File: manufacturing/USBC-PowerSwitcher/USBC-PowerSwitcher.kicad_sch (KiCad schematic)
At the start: 0 parts

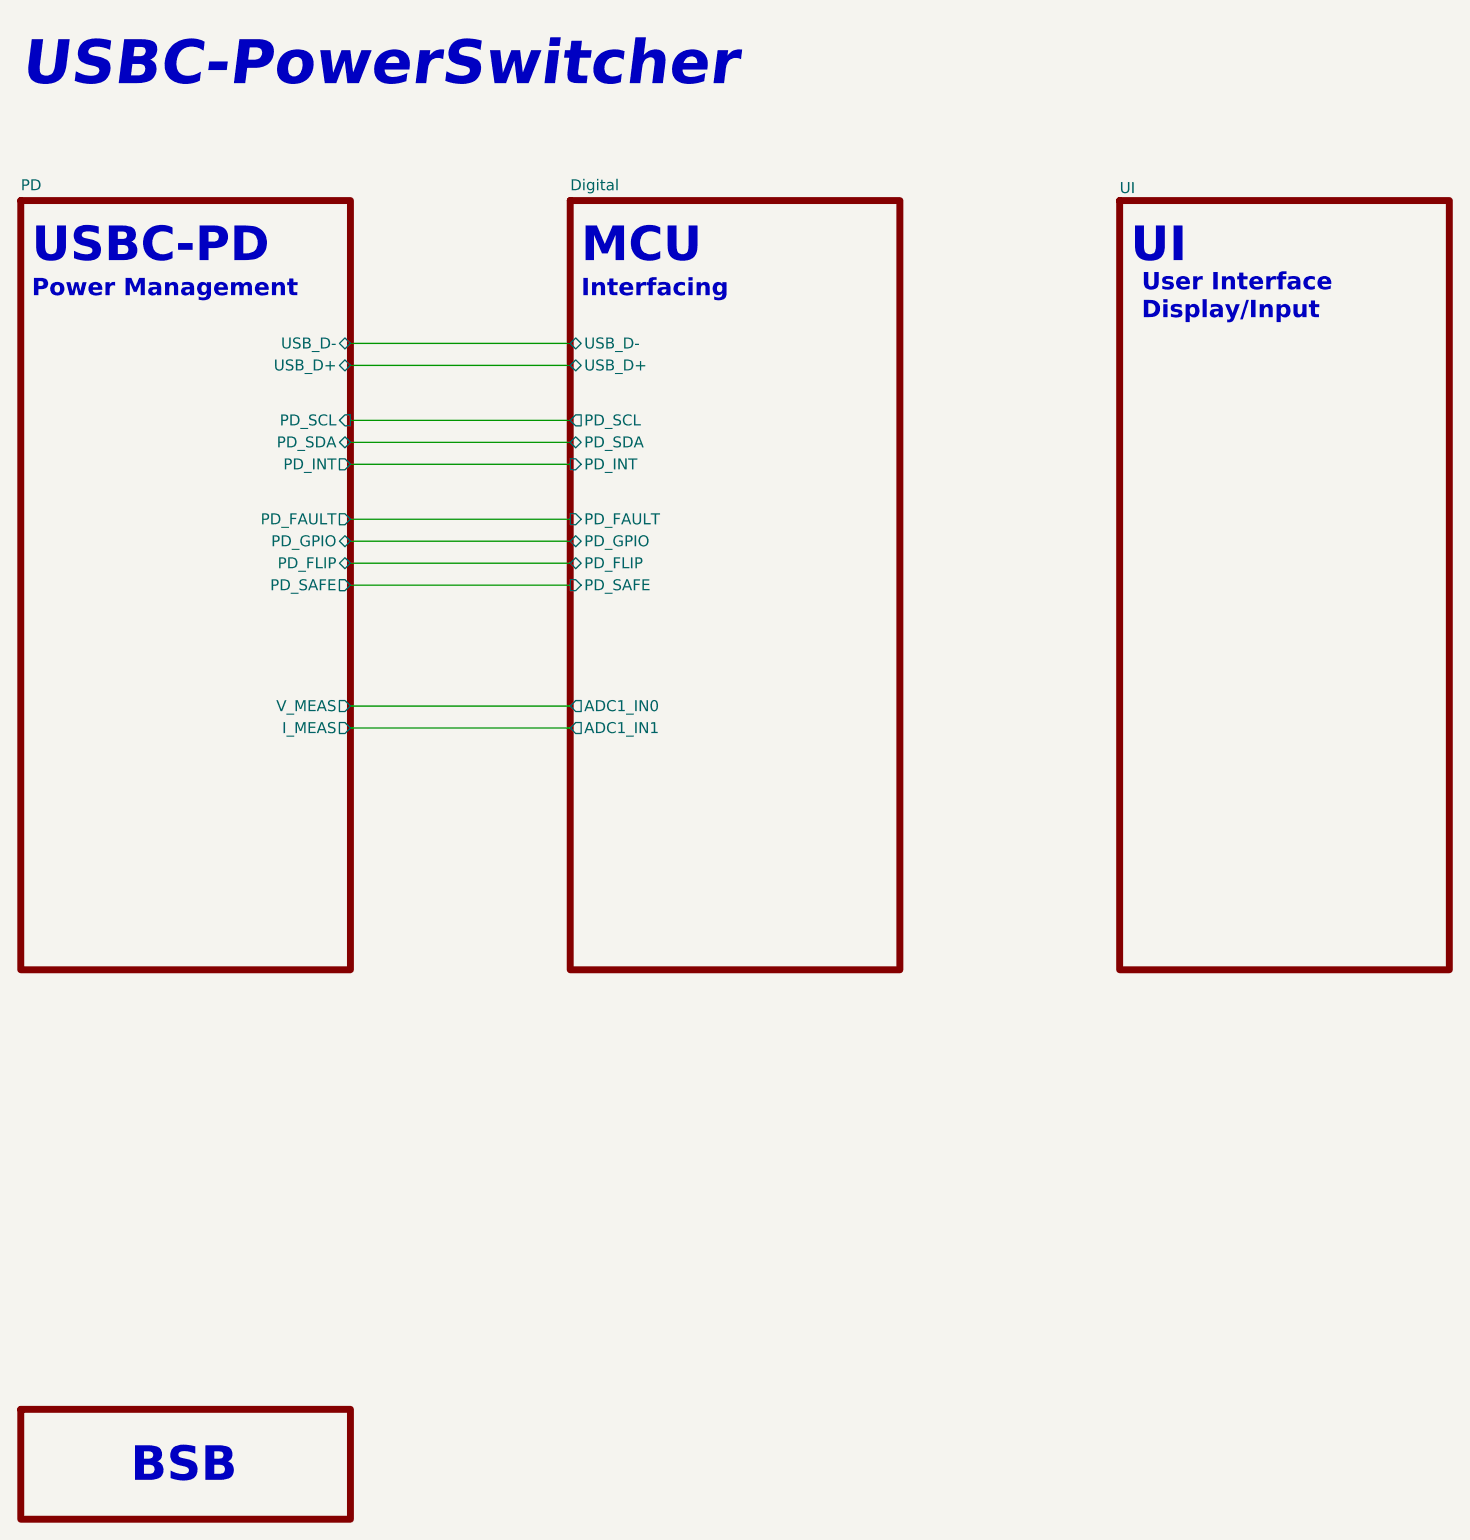
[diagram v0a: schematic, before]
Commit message: First Rough placement
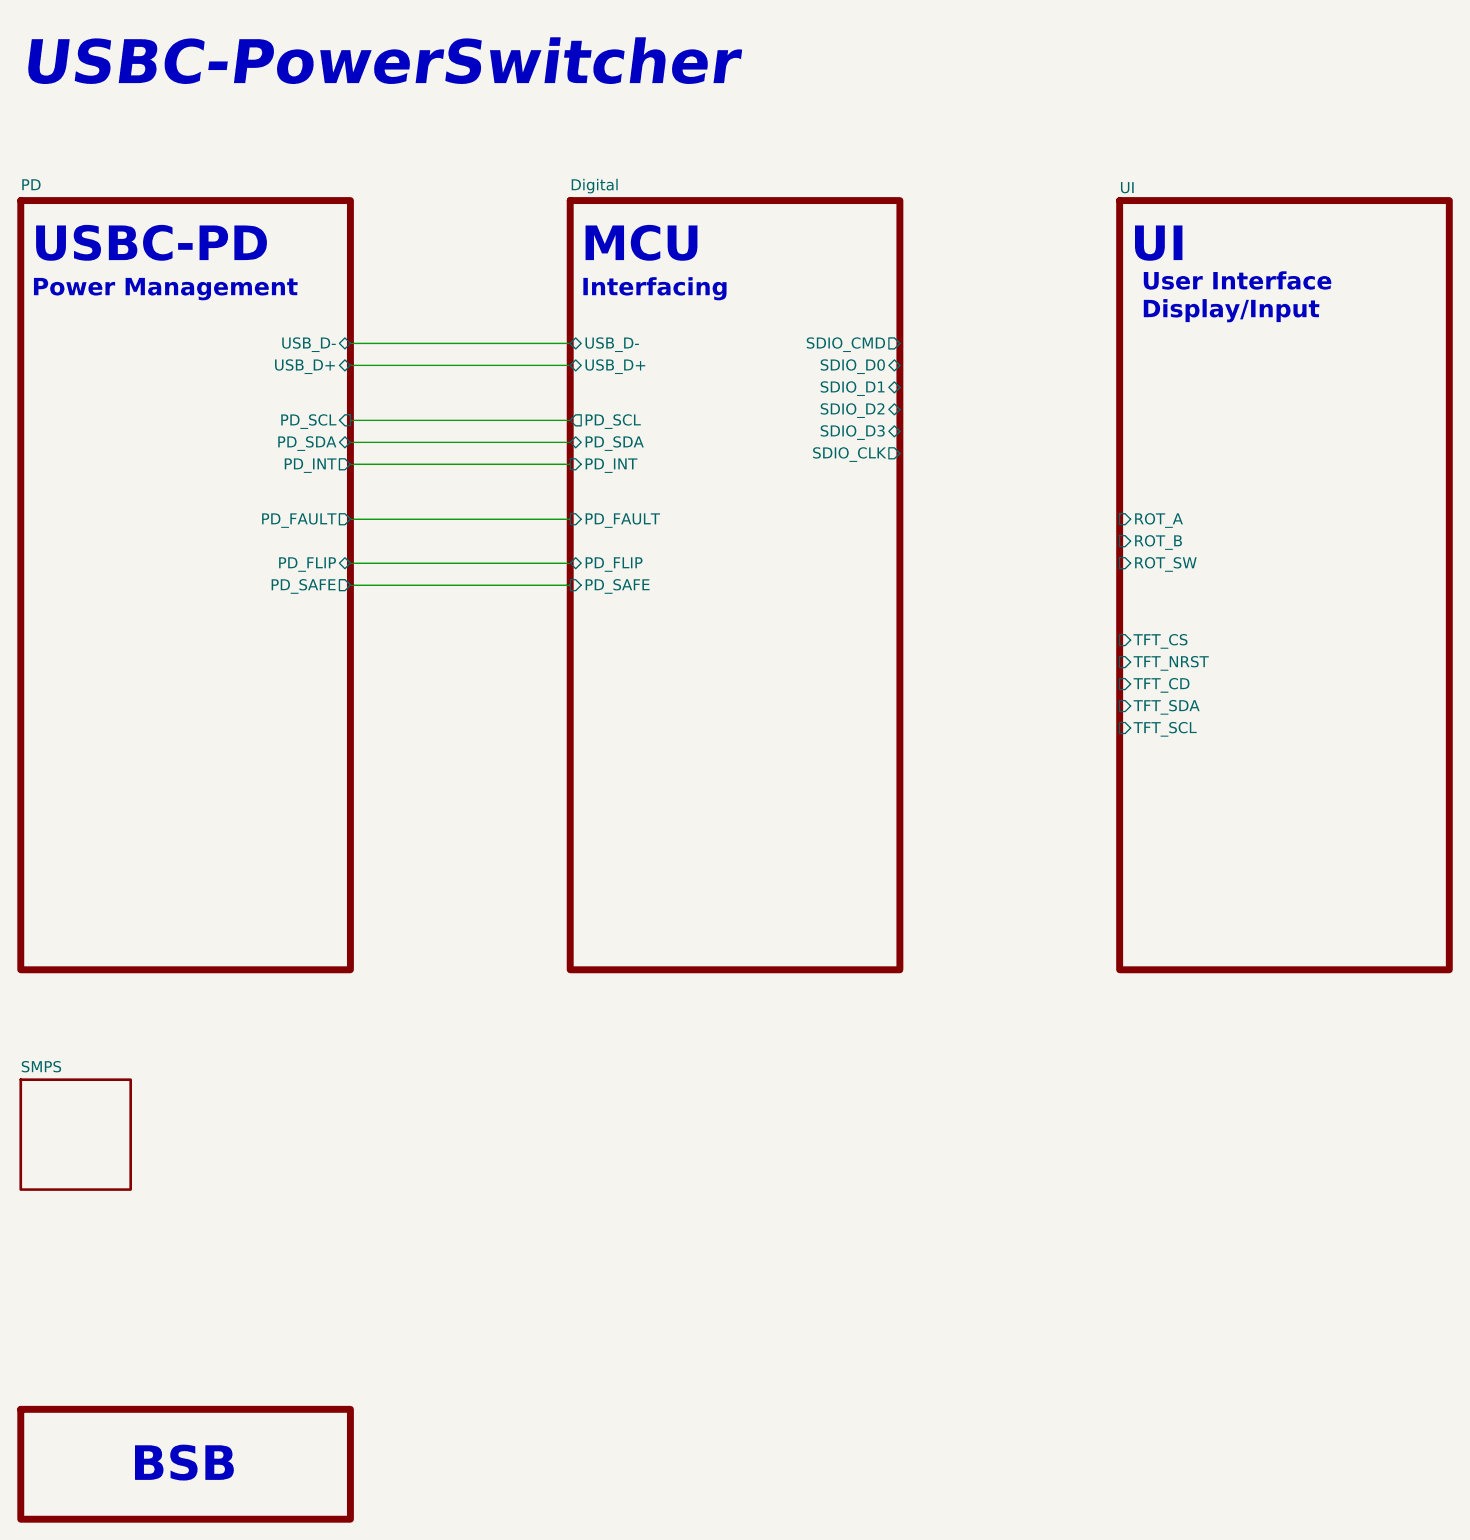
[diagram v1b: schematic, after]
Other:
- added sheet SMPS (SMPS.kicad_sch)
- sheet Digital ports: added SDIO_CLK, SDIO_CMD, SDIO_D0, SDIO_D1, SDIO_D2, SDIO_D3; removed ADC1_IN0, ADC1_IN1, PD_GPIO
- sheet PD ports: added none; removed I_MEAS, PD_GPIO, V_MEAS
- sheet UI ports: added ROT_A, ROT_B, ROT_SW, TFT_CD, TFT_CS, TFT_NRST, TFT_SCL, TFT_SDA; removed none
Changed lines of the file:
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@@
-    (stroke (width 0) (type default))
-  )
-  (wire (pts (xy 63.5 77.47) (xy 88.9 77.47))
     (stroke (width 0) (type default))
   )
   (wire (pts (xy 63.5 74.93) (xy 88.9 74.93))
-    (stroke (width 0) (type default))
-  )
-  (wire (pts (xy 63.5 96.52) (xy 88.9 96.52))
-    (stroke (width 0) (type default))
-  )
-  (wire (pts (xy 63.5 99.06) (xy 88.9 99.06))
     (stroke (width 0) (type default))
   )
@@
       (effects (font (size 1.27 1.27)) (justify right))
     )
-    (pin "PD_GPIO" bidirectional (at 63.5 77.47 0)
-      (effects (font (size 1.27 1.27)) (justify right))
-    )
     (pin "PD_FLIP" tri_state (at 63.5 80.01 0)
       (effects (font (size 1.27 1.27)) (justify right))
@@
     )
     (pin "USB_D+" bidirectional (at 63.5 57.15 0)
-      (effects (font (size 1.27 1.27)) (justify right))
-    )
-    (pin "I_MEAS" output (at 63.5 99.06 0)
-      (effects (font (size 1.27 1.27)) (justify right))
-    )
-    (pin "V_MEAS" output (at 63.5 96.52 0)
       (effects (font (size 1.27 1.27)) (justify right))
     )
@@
     )
   )
+  (sheet (at 25.4 139.7) (size 12.7 12.7) (fields_autoplaced)
+    (stroke (width 0.3) (type solid) (color 125 54 172 1))
+    (fill (color 211 159 255 1.0000))
+    (property "Sheetname" "SMPS" (at 25.4 138.9884 0)
+      (effects (font (size 1.27 1.27)) (justify left bottom))
+    )
+    (property "Sheetfile" "SMPS.kicad_sch" (at 25.4 152.9846 0)
+      (effects (font (size 1.27 1.27)) (justify left top) hide)
+    )
+    (instances
+      (project "USBC-PowerSwitcher"
+        (path "/8eb7596d-c730-4f2a-8fa8-bbe4d7c52643/2ef5b3fe-94be-4def-812a-946a7dedf051" (page "10"))
+        (path "/8eb7596d-c730-4f2a-8fa8-bbe4d7c52643" (page "6"))
+      )
+    )
+  )
   (sheet (at 152.4 38.1) (size 38.1 88.9) (fields_autoplaced)
     (stroke (width 0.8) (type solid) (color 86 81 126 1))
@@
     (property "Sheetfile" "UI.kicad_sch" (at 152.4 127.5846 0)
       (effects (font (size 1.27 1.27)) (justify left top) hide)
+    )
+    (pin "ROT_B" input (at 152.4 77.47 180)
+      (effects (font (size 1.27 1.27)) (justify left))
+    )
+    (pin "ROT_A" input (at 152.4 74.93 180)
+      (effects (font (size 1.27 1.27)) (justify left))
+    )
+    (pin "TFT_CS" input (at 152.4 88.9 180)
+      (effects (font (size 1.27 1.27)) (justify left))
+    )
+    (pin "TFT_NRST" input (at 152.4 91.44 180)
+      (effects (font (size 1.27 1.27)) (justify left))
+    )
+    (pin "TFT_CD" input (at 152.4 93.98 180)
+      (effects (font (size 1.27 1.27)) (justify left))
+    )
+    (pin "TFT_SDA" input (at 152.4 96.52 180)
+      (effects (font (size 1.27 1.27)) (justify left))
+    )
+    (pin "TFT_SCL" input (at 152.4 99.06 180)
+      (effects (font (size 1.27 1.27)) (justify left))
+    )
+    (pin "ROT_SW" input (at 152.4 80.01 180)
+      (effects (font (size 1.27 1.27)) (justify left))
     )
     (instances
@@
       (effects (font (size 1.27 1.27)) (justify left))
     )
-    (pin "ADC1_IN0" output (at 88.9 96.52 180)
-      (effects (font (size 1.27 1.27)) (justify left))
-    )
-    (pin "ADC1_IN1" output (at 88.9 99.06 180)
-      (effects (font (size 1.27 1.27)) (justify left))
-    )
-    (pin "PD_GPIO" bidirectional (at 88.9 77.47 180)
-      (effects (font (size 1.27 1.27)) (justify left))
-    )
     (pin "PD_FAULT" input (at 88.9 74.93 180)
       (effects (font (size 1.27 1.27)) (justify left))
@@
       (effects (font (size 1.27 1.27)) (justify left))
     )
+    (pin "SDIO_CMD" output (at 127 54.61 0)
+      (effects (font (size 1.27 1.27)) (justify right))
+    )
+    (pin "SDIO_D0" bidirectional (at 127 57.15 0)
+      (effects (font (size 1.27 1.27)) (justify right))
+    )
+    (pin "SDIO_CLK" output (at 127 67.31 0)
+      (effects (font (size 1.27 1.27)) (justify right))
+    )
+    (pin "SDIO_D2" bidirectional (at 127 62.23 0)
+      (effects (font (size 1.27 1.27)) (justify right))
+    )
+    (pin "SDIO_D1" bidirectional (at 127 59.69 0)
+      (effects (font (size 1.27 1.27)) (justify right))
+    )
+    (pin "SDIO_D3" bidirectional (at 127 64.77 0)
+      (effects (font (size 1.27 1.27)) (justify right))
+    )
     (instances
